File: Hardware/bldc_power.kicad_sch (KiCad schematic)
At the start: 33 parts, among them U3 DRV8302

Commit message: close to 1st done
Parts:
- removed C34, C36: 2.2n, Capacitor_SMD:C_0603_1608Metric, symbol BLDC_4-rescue:C-RESCUE-BLDC_4
- removed R48, R49, R50, R51: 100R, Resistor_SMD:R_0603_1608Metric, symbol BLDC_4-rescue:R-RESCUE-BLDC_4
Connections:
- net SP2: now reaches U3.30 (SP2)
- net SN2: now reaches U3.31 (SN2)
- net SP1: now reaches U3.32 (SP1)
- net SN1: now reaches U3.33 (SN1)
- net H1_LOW renamed SL_A
- net H1_VS renamed SH_A
- net H2_LOW renamed SL_B
- net H2_VS renamed SH_B
- net H3_LOW renamed SL_C
- net H3_VS renamed SH_C
- net M_H1 renamed GH_A
- net M_H2 renamed GH_B
- net M_H3 renamed GH_C
- net M_L1 renamed GL_A
- net M_L2 renamed GL_B
- net M_L3 renamed GL_C

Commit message: final touches and adding encoder
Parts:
- added C24, C25, C33, C34: 10u,50V, Capacitor_SMD:C_1206_3216Metric, symbol BLDC_4-rescue:C-RESCUE-BLDC_4
- added C27, C36: 15u, 100v, Capacitor_SMD:C_2220_5750Metric, symbol BLDC_4-rescue:C-RESCUE-BLDC_4
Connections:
- net GND: now also C24.1, C25.1, C27.1, C33.1, C34.1, C36.1
- net V_SUPPLY: now also C24.2, C25.2, C27.2, C33.2, C34.2, C36.2

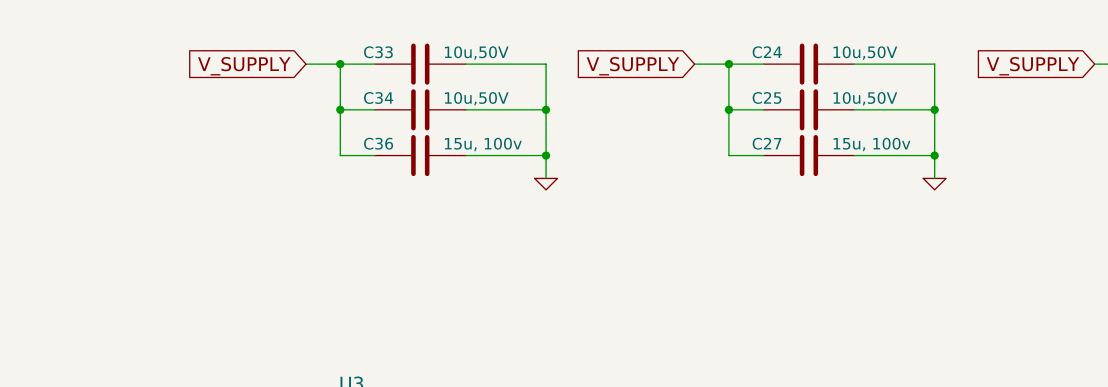
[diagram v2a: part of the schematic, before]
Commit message: removed some decoupling caps from sims
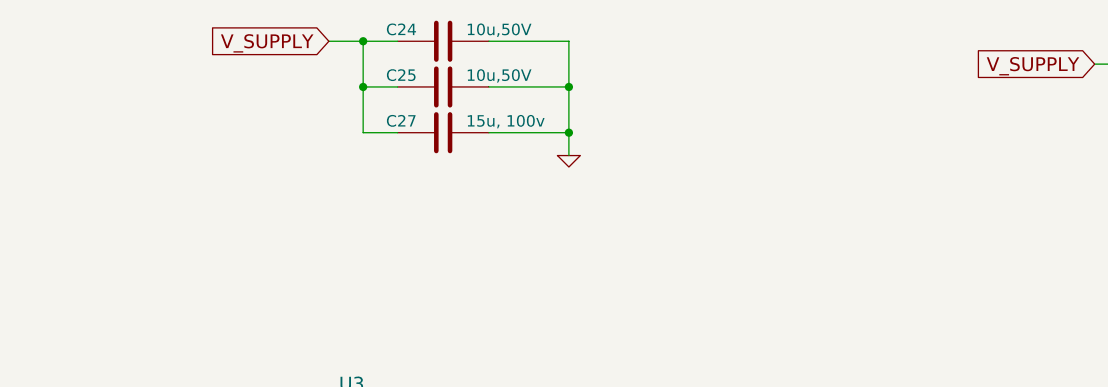
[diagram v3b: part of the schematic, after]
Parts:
- removed C33, C34: 10u,50V, Capacitor_SMD:C_1206_3216Metric, symbol BLDC_4-rescue:C-RESCUE-BLDC_4
- removed C36: 15u, 100v, Capacitor_SMD:C_2220_5750Metric, symbol BLDC_4-rescue:C-RESCUE-BLDC_4
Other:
- moved on the sheet: C24, C25, C27

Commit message: changes made post will's review
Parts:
- removed C1, C24, C25, C40, C43, C44, C49, C8, C9: 10u,50V, Capacitor_SMD:C_1206_3216Metric, symbol BLDC_4-rescue:C-RESCUE-BLDC_4
- removed C18, C20, C23, C26, C52: 2.2u, Capacitor_SMD:C_0603_1608Metric, symbol BLDC_4-rescue:C-RESCUE-BLDC_4
- removed C22: 22n, Capacitor_SMD:C_0603_1608Metric, symbol BLDC_4-rescue:C-RESCUE-BLDC_4
- removed C27, C51: 15u, 100v, Capacitor_SMD:C_2220_5750Metric, symbol BLDC_4-rescue:C-RESCUE-BLDC_4
- removed C28, C29, C30: 220n, Capacitor_SMD:C_0603_1608Metric, symbol BLDC_4-rescue:C-RESCUE-BLDC_4
- removed C37: 15u,100V, Capacitor_SMD:C_2220_5750Metric, symbol BLDC_4-rescue:C-RESCUE-BLDC_4
- removed R20: 10k, Resistor_SMD:R_0402_1005Metric, symbol BLDC_4-rescue:R-RESCUE-BLDC_4
- removed R23, R26, R32: 39k, Resistor_SMD:R_0603_1608Metric, symbol BLDC_4-rescue:R-RESCUE-BLDC_4
- removed R24, R27, R33: 2k2, Resistor_SMD:R_0402_1005Metric, symbol BLDC_4-rescue:R-RESCUE-BLDC_4
- removed R25: 1M, Resistor_SMD:R_0603_1608Metric, symbol BLDC_4-rescue:R-RESCUE-BLDC_4
- added C601: 2.2uF, Capacitor_SMD:C_0402_1005Metric, symbol Device:C_Small
- added C602, C606: 1uF, Capacitor_SMD:C_0402_1005Metric, symbol Device:C_Small
- added C603, C604, C608, C609, C612, C616, C617: 10uF, 50V, Capacitor_SMD:C_1206_3216Metric, symbol Device:C_Small
- added C605, C610, C618: 15uF, 100V, Capacitor_SMD:C_2220_5750Metric, symbol Device:C_Small
- added C607: 22nF, 50V, Capacitor_SMD:C_0402_1005Metric, symbol Device:C_Small
- added C611: 100nF, 50V, Capacitor_SMD:C_0603_1608Metric, symbol Device:C_Small
- added C613, C614, C615: 220nF, 50V, Capacitor_SMD:C_0402_1005Metric, symbol Device:C_Small
- added R601, R602: ~, Resistor_SMD:R_0402_1005Metric, symbol Device:R_Small
- added R603, R604, R605: 10kΩ, Resistor_SMD:R_0402_1005Metric, symbol Device:R_Small
- added R606: 1MΩ, Resistor_SMD:R_0402_1005Metric, symbol Device:R_Small
- added R607, R609, R611: 39kΩ, Resistor_SMD:R_0402_1005Metric, symbol Device:R_Small
- added R608, R610, R612: 2.2kΩ, Resistor_SMD:R_0402_1005Metric, symbol Device:R_Small
- renumbered U3 to U601
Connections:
- net FAULT: now also R603.1
- net GND: now also C601.2, C603.1, C604.1, C605.1, C608.1, C609.1, C610.1, C611.2, C612.2, C616.1, C617.1, C618.1, R602.1, R604.1, R606.2, R608.2, R610.2, R612.2; no longer U601.28 (AGND)
- net SENS1: now also R607.1, R608.1
- net SENS2: now also R609.1, R610.1
- net SENS3: now also R611.1, R612.1
- net SH_A: now also C614.1, R611.2
- net SH_B: now also C613.1, R609.2
- net SH_C: now also C615.1, R607.2
- net V_SUPPLY: now also C603.2, C604.2, C605.2, C608.2, C609.2, C610.2, C611.1, C612.1, C616.2, C617.2, C618.2
- net at U601.48 (BST_A): now also C614.2
- net at U601.11 (OC_ADJ): now also R601.1, R602.2; no longer U601.23 (DVDD)
- net at U601.13 (GVDD): now also C601.1
- net at U601.14 (CP1): now also C607.1
- net at U601.15 (CP2): now also C607.2
- net at U601.27 (AVDD): now also C606.2
- net at U601.38 (BST_C): now also C615.2
- net at U601.43 (BST_B): now also C613.2
- net at U601.49 (BIAS): now also R606.1
- net OCTW: now reaches U601.5 (OCTW)
- net OCTW: now also R605.1
- net at U601.7 (DTC): now also R604.2
- net VCC renamed +3V3
- net +3V3: now also R601.2, R603.2, R605.2
- new net: C602.1, U601.23 (DVDD)
- new net AGND: C602.2, C606.1, U601.28 (AGND)
- no-connect marks 12 -> 11
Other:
- note added: "Put 2 220uF electrolytic caps on the board somewhere"
